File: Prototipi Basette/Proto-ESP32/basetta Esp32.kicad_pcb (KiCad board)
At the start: 2 copper layers, 66 x 55.9 mm, 8 parts, among them J1 Conn_01x19, J2 Conn_01x19, J3 Conn_01x19, J4 Conn_01x19, U1 L7805

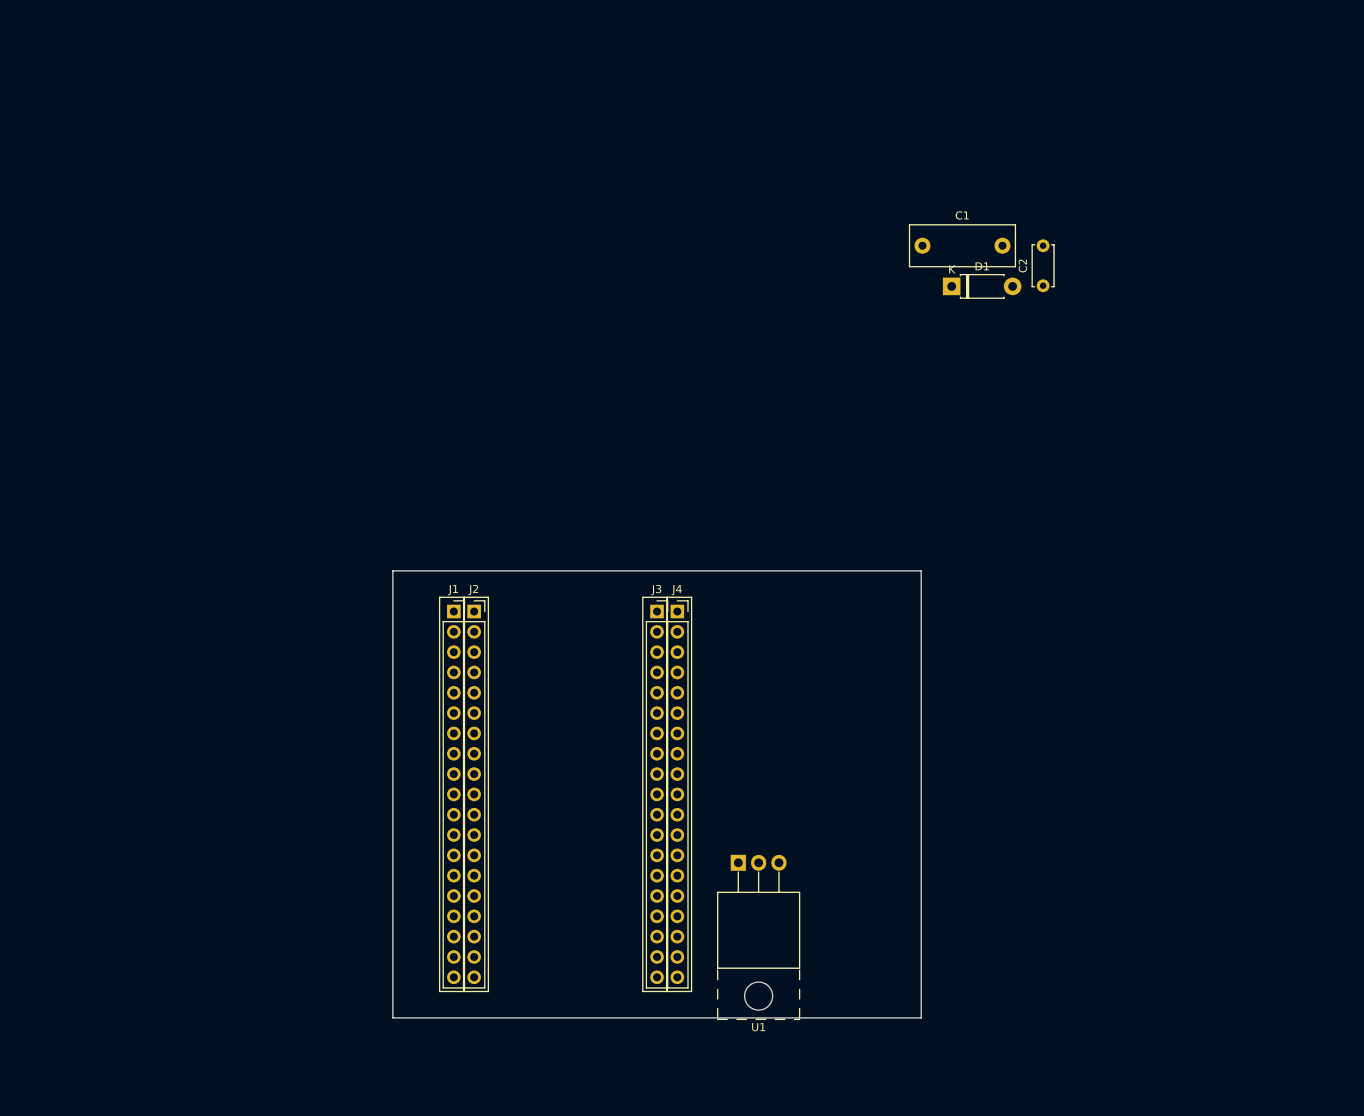
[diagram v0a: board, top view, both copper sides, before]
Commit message: Add LM2596 symbol/footprint and update PCB
Add LM2596 footprint and symbol libraries, update project schematic and PCB files, and refresh project metadata. Includes new Library.pretty/LM2596 - IC footprint, Simboli_Progetto.* symbol library files, updated basetta Esp32.kicad_pcb/.kicad_sch/.kicad_pro/.kicad_prl and fp-info-cache, plus fp-lib-table and sym-lib-table. Several backup ZIPs were removed and replaced with new timestamped backups, and freerouting/temp freerouting files and a freerouting plugin ZIP were added.
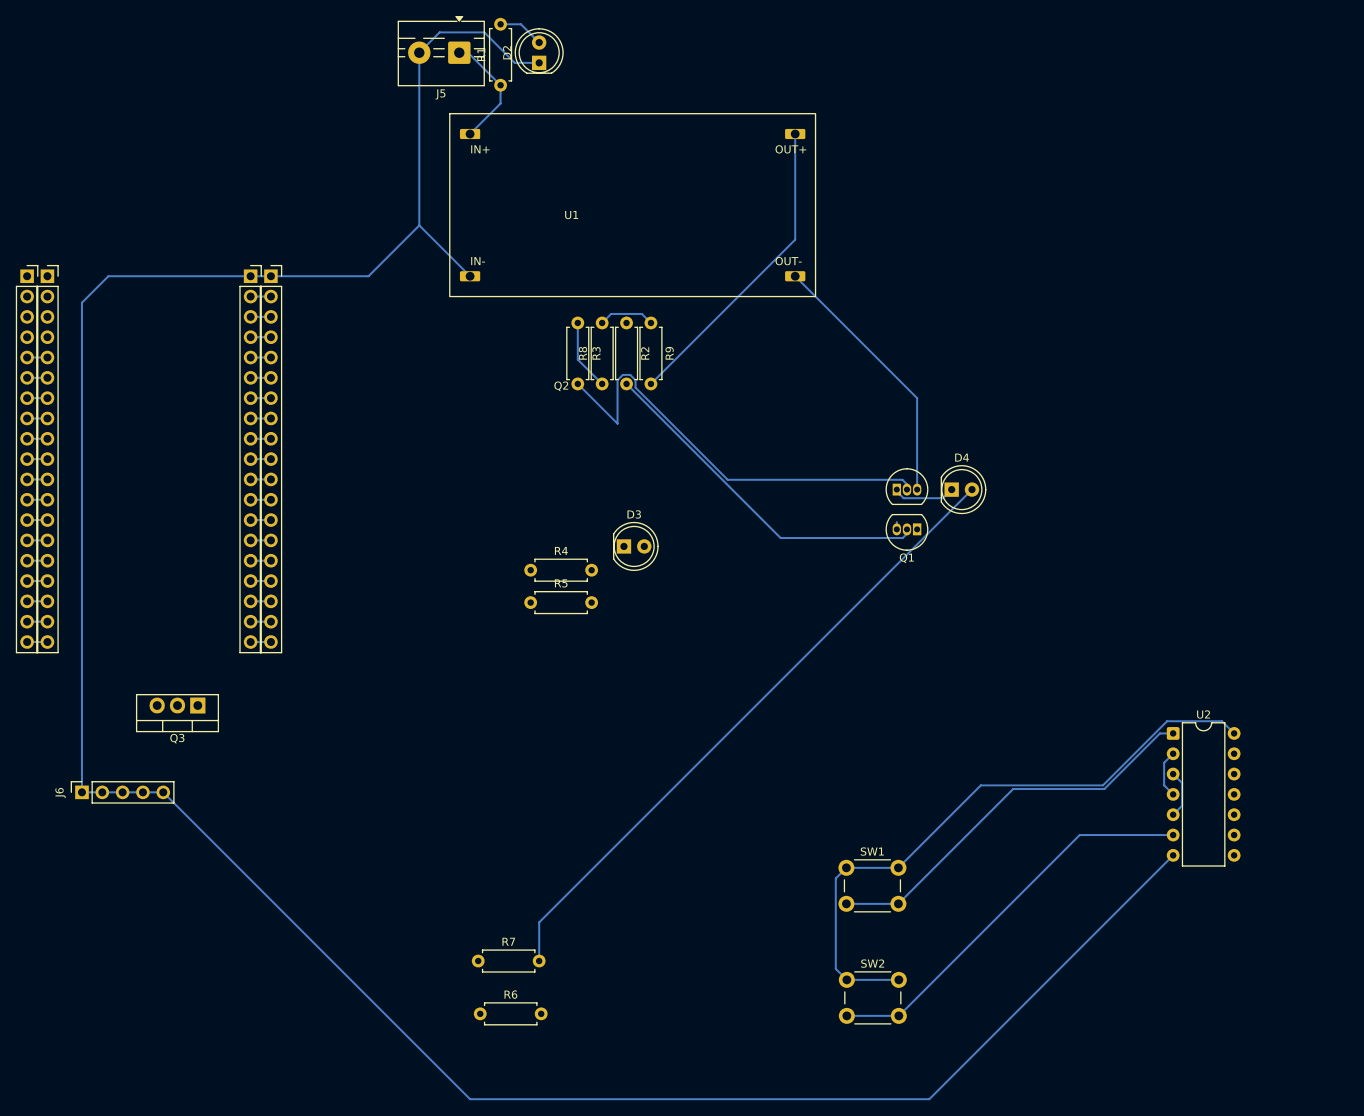
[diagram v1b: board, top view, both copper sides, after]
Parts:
- removed C1: C, Capacitor_THT:C_Rect_L13.0mm_W5.0mm_P10.00mm_FKS3_FKP3_MKS4
- removed C2: C, Capacitor_THT:C_Disc_D5.0mm_W2.5mm_P5.00mm
- removed D1: 1N4007, Diode_THT:D_DO-41_SOD81_P7.62mm_Horizontal
- added D2: LED, LED_THT:LED_D5.0mm, F.Cu at (99.6, 30.5)
- added D3: ESP32 ON, LED_THT:LED_D5.0mm, F.Cu at (110.2, 90.9)
- added D4: ESP32 OFF, LED_THT:LED_D5.0mm, F.Cu at (151.1, 83.8)
- added J5: Screw_Terminal_01x02, TerminalBlock:TerminalBlock_MaiXu_MX126-5.0-02P_1x02_P5.00mm, F.Cu at (89.6, 29.2)
- added J6: Conn_01x05, Connector_PinSocket_2.54mm:PinSocket_1x05_P2.54mm_Vertical, F.Cu at (42.4, 121.7)
- added Q1: BC547, Package_TO_SOT_THT:TO-92_Inline, F.Cu at (146.8, 88.8)
- added Q2: BC547, Package_TO_SOT_THT:TO-92_Inline, F.Cu at (144.3, 83.8)
- added Q3: IRF9540N, Package_TO_SOT_THT:TO-220-3_Vertical, F.Cu at (56.9, 110.8)
- added R1: R, Resistor_THT:R_Axial_DIN0207_L6.3mm_D2.5mm_P7.62mm_Horizontal, F.Cu at (94.7, 33.3)
- added R2: 4.7 k, Resistor_THT:R_Axial_DIN0207_L6.3mm_D2.5mm_P7.62mm_Horizontal, F.Cu at (110.5, 63.0)
- added R3: 4.7 k, Resistor_THT:R_Axial_DIN0207_L6.3mm_D2.5mm_P7.62mm_Horizontal, F.Cu at (104.4, 63.0)
- added R4: 10k, Resistor_THT:R_Axial_DIN0207_L6.3mm_D2.5mm_P7.62mm_Horizontal, F.Cu at (98.5, 93.9)
- added R5: 10k, Resistor_THT:R_Axial_DIN0207_L6.3mm_D2.5mm_P7.62mm_Horizontal, F.Cu at (98.5, 97.9)
- added R6: 470, Resistor_THT:R_Axial_DIN0207_L6.3mm_D2.5mm_P7.62mm_Horizontal, F.Cu at (92.2, 149.4)
- added R7: 470, Resistor_THT:R_Axial_DIN0207_L6.3mm_D2.5mm_P7.62mm_Horizontal, F.Cu at (91.9, 142.7)
- added R8: 470, Resistor_THT:R_Axial_DIN0207_L6.3mm_D2.5mm_P7.62mm_Horizontal, F.Cu at (107.4, 70.6)
- added R9: 10k, Resistor_THT:R_Axial_DIN0207_L6.3mm_D2.5mm_P7.62mm_Horizontal, F.Cu at (113.5, 63.0)
- added SW1: RESET, Button_Switch_THT:SW_PUSH_6mm_H4.3mm, F.Cu at (138.0, 131.1)
- added SW2: SET, Button_Switch_THT:SW_PUSH_6mm_H4.3mm, F.Cu at (138.0, 145.1)
- added U2: 4001, Package_DIP:DIP-14_W7.62mm, F.Cu at (178.8, 114.3)
- U1: value L7805 -> ~; footprint Package_TO_SOT_THT:TO-220-3_Horizontal_TabUp -> Library:LM2596 - IC
- moved U1 80.6 mm to (90.9, 57.1)
- moved J1 67.8 mm to (35.6, 57.1)
- moved J2 67.8 mm to (38.1, 57.1)
- moved J3 65.9 mm to (63.5, 57.1)
- moved J4 65.9 mm to (66.0, 57.1)
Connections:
- net Net-(J1-Pin_4) renamed ESP-32 POW
- U1 pad 1: Net-(D1-K) -> V_in_Batterie
- U1 pad 3: Net-(D1-A) -> 5 V
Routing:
- net GND: track 0.00 -> 354.6 mm
- net 5 V: track 0.00 -> 117.0 mm
- net Net-(D4-A): track 0.00 -> 81.3 mm
- net Net-(Q2-B): track 0.00 -> 55.8 mm
- net Net-(R5-Pad1): track 0.00 -> 50.2 mm
- net Net-(R4-Pad1): track 0.00 -> 49.7 mm
- net Net-(Q1-B): track 0.00 -> 43.8 mm
- net SIGN_ESP32: track 0.00 -> 14.9 mm
- net V_in_Batterie: track 0.00 -> 14.5 mm
- net Net-(D4-K): track 0.00 -> 7.88 mm
- net Net-(Q3-G): track 0.00 -> 7.39 mm
- net Net-(R2-Pad1): track 0.00 -> 6.01 mm
- net Net-(D2-A): track 0.00 -> 5.77 mm
- net Net-(J3-Pin_9): track 0.00 -> 2.54 mm
- net Net-(J3-Pin_8): track 0.00 -> 2.54 mm
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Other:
- board outline removed
- board text added: "IN+"
- board text removed: "Alimentazione"

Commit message: Update ESP32 board files and docs
Add compiled Arduino/main.pdf and simplify Arduino/pulsante.tex (remove blocking debouncing example and tidy Bounce2 section). Add several timestamped basetta Esp32 backup ZIPs. Large KiCad changes to basetta Esp32: update .kicad_pcb footprints, pads, nets and 3D models (replace/adjust LED/resistor footprints, add 1x19 pin socket connector, LM2596 module, DIP U3 and many pads; adjust silk/fab layers, pad geometry and UUIDs), and update related project files (.kicad_sch, .kicad_prl, freerouting.dsn and temp-freerouting.dsn). These changes refine the schematic/PCB layout and capture incremental backups.
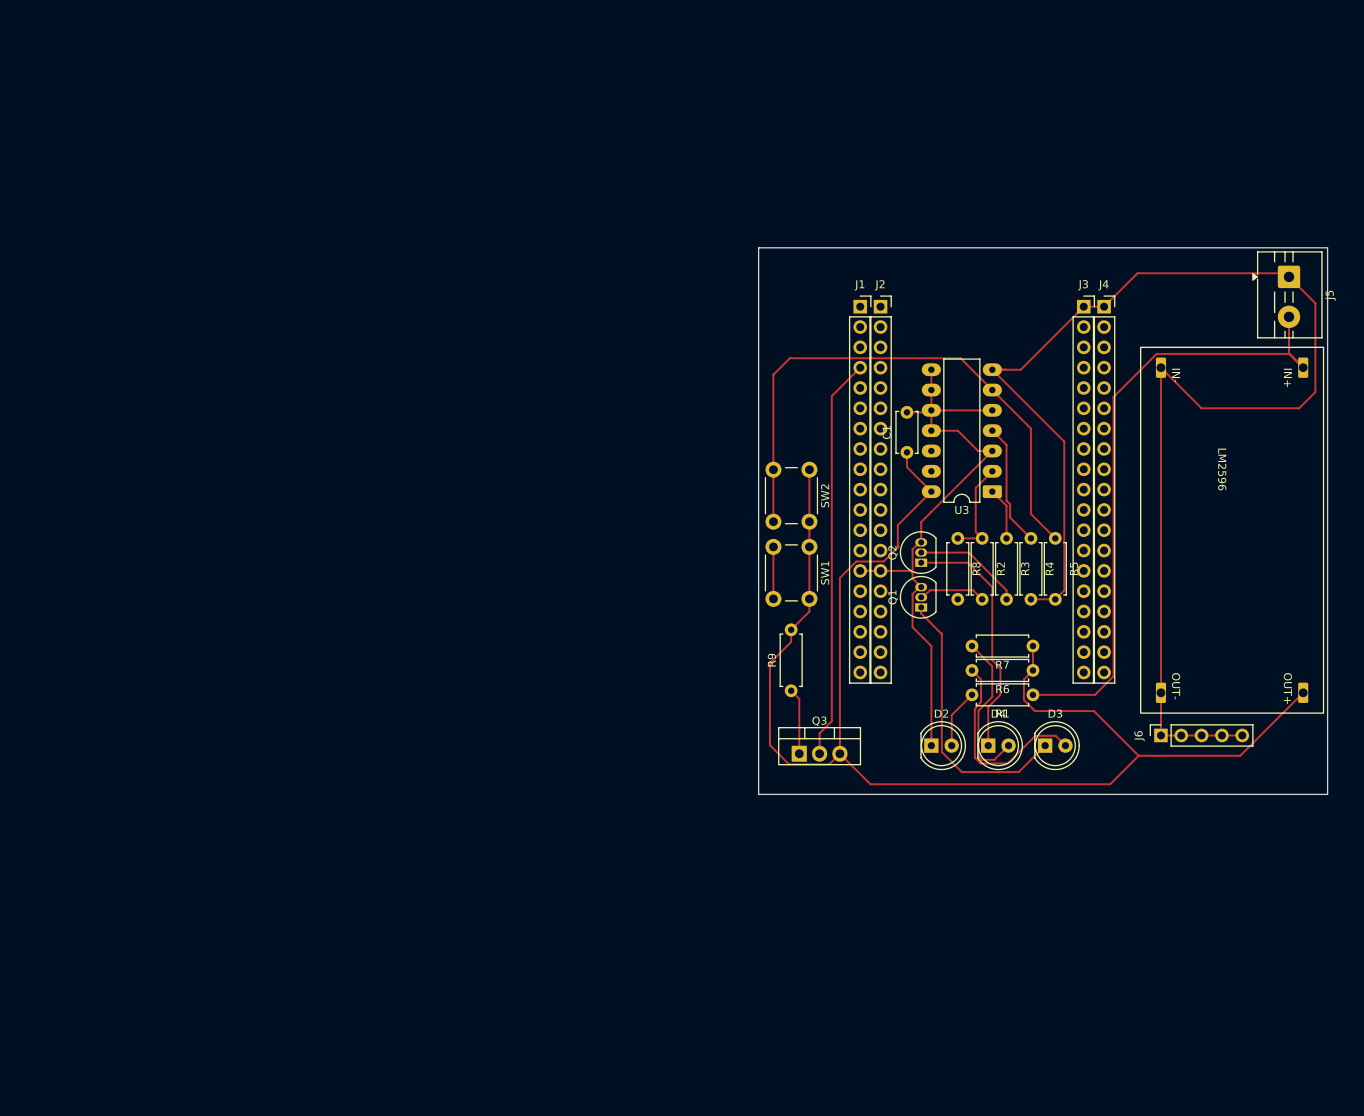
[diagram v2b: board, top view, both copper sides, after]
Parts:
- removed U1: ~, Library:LM2596 - IC
- removed U2: 4001, Package_DIP:DIP-14_W7.62mm
- added C1: 100n, Capacitor_THT:C_Disc_D5.0mm_W2.5mm_P5.00mm, F.Cu at (145.5, 79.2)
- added LM2596: ~, Library:LM2596 - IC, F.Cu at (177.3, 68.6)
- added U3: 4013, Package_DIP:DIP-14_W7.62mm_LongPads, F.Cu at (156.2, 84.1)
- D3: value ESP32 ON -> ESP32 OFF
- D4: value ESP32 OFF -> ESP32 ON
- moved J6 135.1 mm to (177.3, 114.6)
- moved J5 107.4 mm to (193.3, 57.2), turned to -90 degrees
- moved J2 104.2 mm to (142.2, 61.0)
- moved J4 104.2 mm to (170.2, 61.0)
- moved J1 104.2 mm to (139.7, 61.0)
- moved J3 104.2 mm to (167.6, 61.0)
- moved R1 101.2 mm to (161.3, 109.5), turned to 180 degrees
- moved D2 98.4 mm to (148.6, 115.8), turned to 0 degrees
- moved R6 81.3 mm to (161.3, 106.4), turned to 180 degrees
- moved R7 79.7 mm to (161.3, 103.4), turned to 180 degrees
- moved Q3 75.4 mm to (132.1, 116.8), turned to 0 degrees
- moved R5 66.1 mm to (164.1, 89.9), turned to -90 degrees
- moved SW2 63.9 mm to (133.3, 81.3), turned to -90 degrees
- moved R4 62.7 mm to (161.0, 89.9), turned to -90 degrees
- moved R3 60.0 mm to (158.0, 89.9)
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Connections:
- J1 pad 14: Net-(J1-Pin_14) -> GND
- J2 pad 14: Net-(J1-Pin_14) -> GND
- J5 pad 1: V_in_Batterie -> GND
- J5 pad 2: GND -> V_in_Batterie
- R2 pad 1: Net-(R2-Pad1) -> SIGN_ESP32
- R3 pad 1: SIGN_ESP32 -> Net-(U3A-Q)
- R6 pad 1: V_in_Batterie -> 5 V
- R7 pad 1: V_in_Batterie -> 5 V
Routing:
- net GND: track 354.6 -> 252.0 mm
- net V_in_Batterie: track 14.5 -> 79.7 mm
- net 5 V: track 117.0 -> 181.7 mm
- net Net-(D4-A): track 81.3 -> 20.2 mm
- net ESP-32 POW: track 0.00 -> 50.4 mm
- net Net-(Q2-B): track 55.8 -> 13.8 mm
- net Net-(Q1-B): track 43.8 -> 8.81 mm
- net Net-(D3-K): track 0.00 -> 34.5 mm
- net Net-(U3A-R): track 49.7 -> 22.0 mm
- net Net-(D3-A): track 0.00 -> 25.3 mm
- net Net-(D4-K): track 7.88 -> 31.0 mm
- net Net-(U3A-S): track 50.2 -> 70.0 mm
- net Net-(U3A-Q): track 0.00 -> 6.58 mm
- net Net-(R2-Pad1): track 6.01 -> 0.00 mm
- net Net-(J3-Pin_9): track 2.54 -> 0.00 mm
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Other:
- board outline added: 71.1 x 68.3 mm
- board text removed: "IN+"

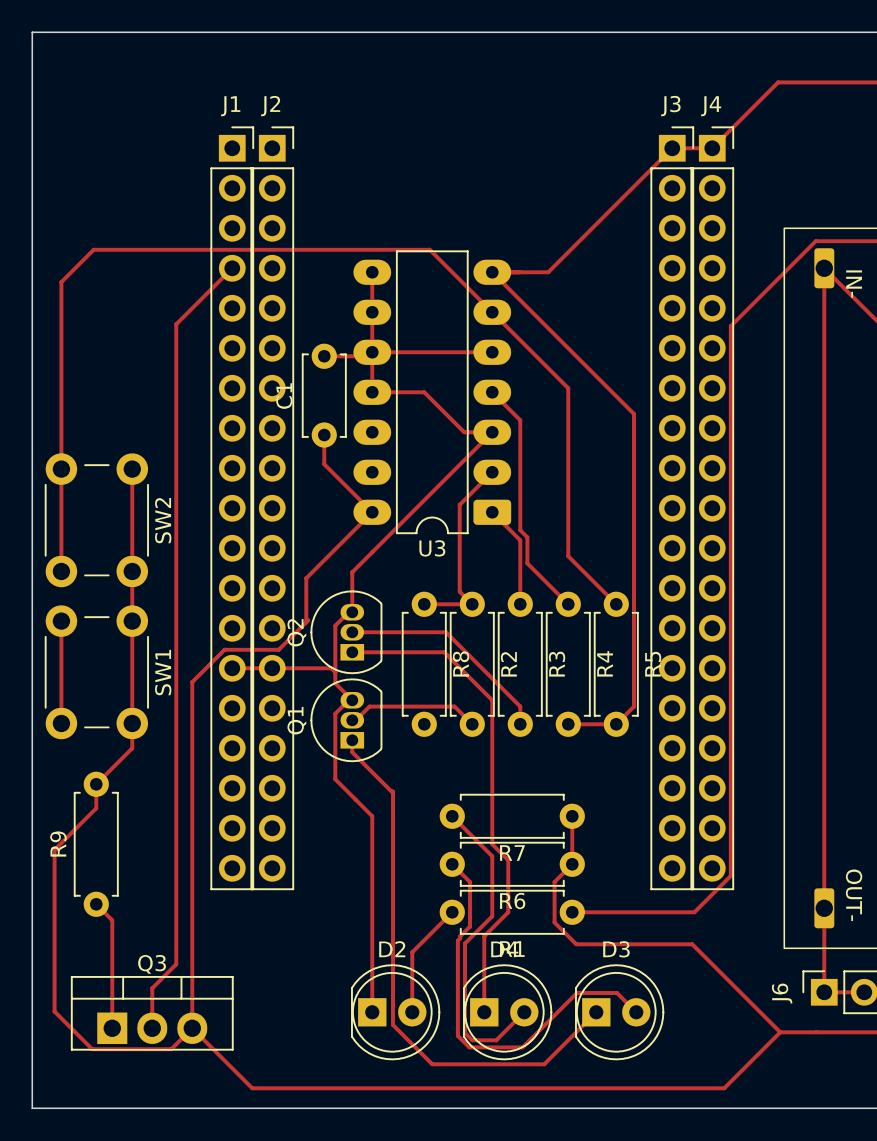
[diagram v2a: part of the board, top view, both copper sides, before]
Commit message: Update KiCad PCB to newer format and footprints
Upgrade basetta Esp32.kicad_pcb to a newer pcbnew/generator version and apply footprint/pad updates. Changes include generator/version bump, expanded setup entries (tenting/covering/plugging), conversion of numeric net ids to named nets, normalized pinfunction names (suffixes added), adjusted footprint positions/orientations and many UUID updates, added unit definitions and duplicate_pad_numbers_are_jumpers flags, and cleaned Datasheet fields. Also add a timestamped backup zip of the project.
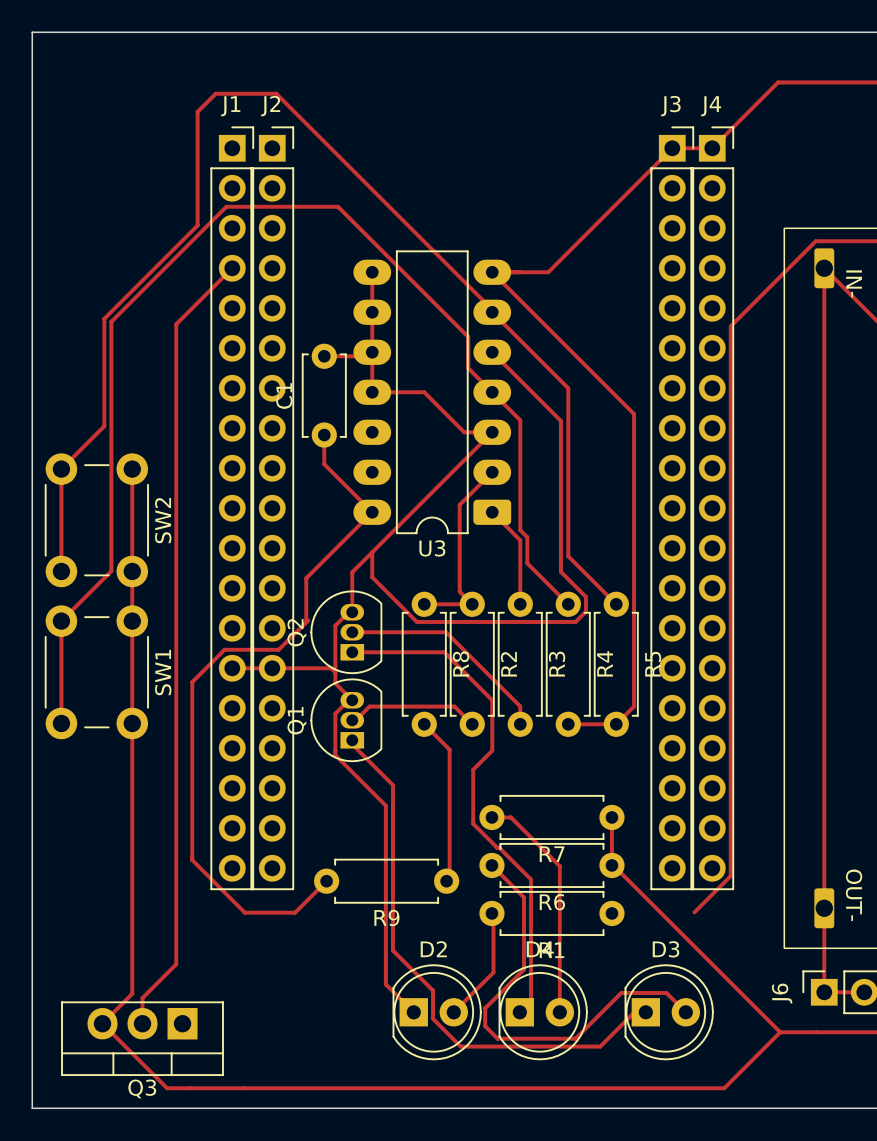
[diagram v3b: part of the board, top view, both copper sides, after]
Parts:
- moved R9 22.3 mm to (153.3, 107.5), turned to 180 degrees
- moved Q3 4.47 mm to (136.5, 116.5), turned to 180 degrees
- moved D3 3.15 mm to (166.0, 115.8)
- moved D2 2.63 mm to (151.2, 115.8)
- moved R1 2.52 mm to (163.8, 109.5)
- moved R6 2.52 mm to (163.8, 106.5)
- moved R7 2.52 mm to (163.8, 103.5)
- moved D4 2.26 mm to (158.0, 115.8)
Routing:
- net Net-(U3A-R): track 22.0 -> 75.5 mm
- net GND: track 252.0 -> 281.0 mm
- net 5 V: track 181.7 -> 170.5 mm
- net Net-(U3A-S): track 70.0 -> 79.6 mm
- net V_in_Batterie: track 79.7 -> 71.9 mm
- net Net-(D4-A): track 20.2 -> 14.9 mm
- net Net-(D4-K): track 31.0 -> 33.5 mm
- net Net-(Q3-G): track 9.01 -> 10.9 mm
- net Net-(D3-A): track 25.3 -> 26.8 mm
